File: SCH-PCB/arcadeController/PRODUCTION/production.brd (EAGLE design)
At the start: 120.9 x 92.9 mm, 52 parts, among them J1 1759046, J2 1759046, J3 1759046, J4 1759046, J5 1759046, J6 1759046, J7 1759046, J8 1759046, U1 RASPBERRY_PICOSMD-TH, U2 RASPBERRY_PICOSMD-TH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

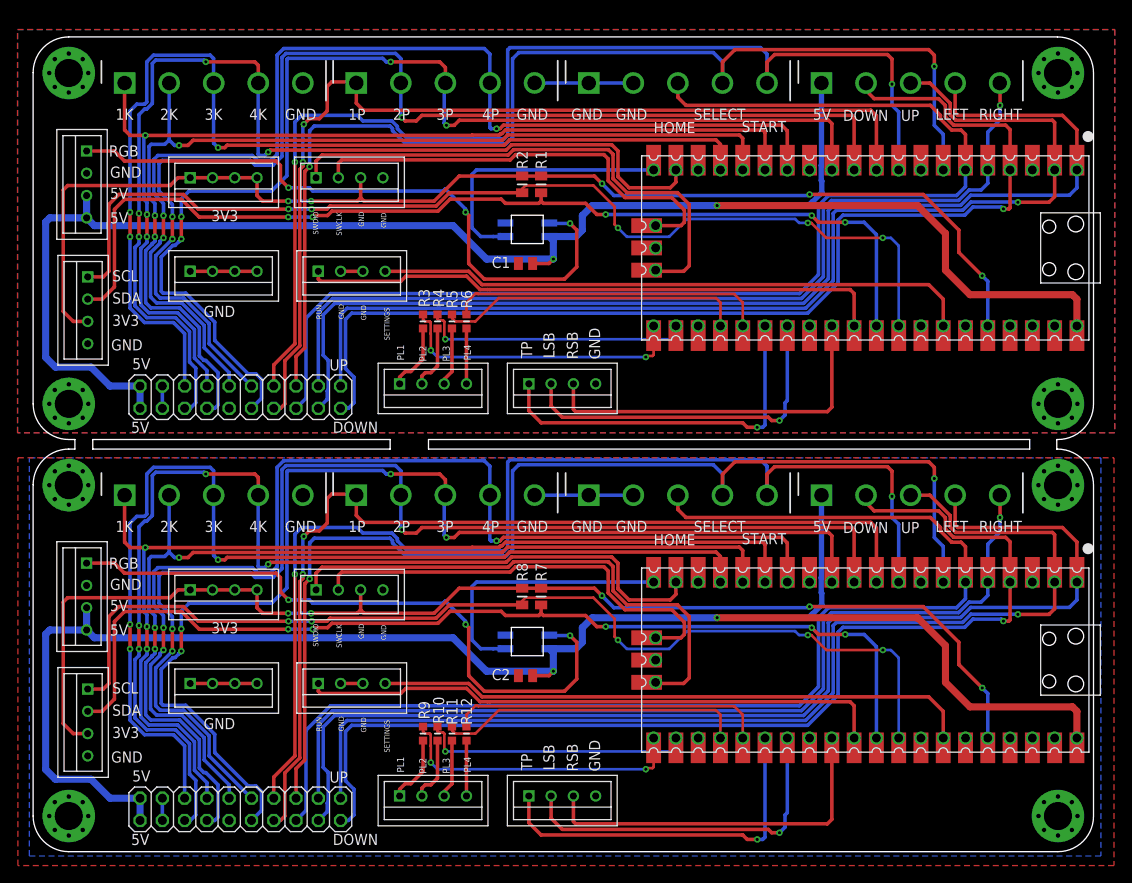
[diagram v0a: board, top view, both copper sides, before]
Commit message: FIX: PCB design there are line with <0.1mm
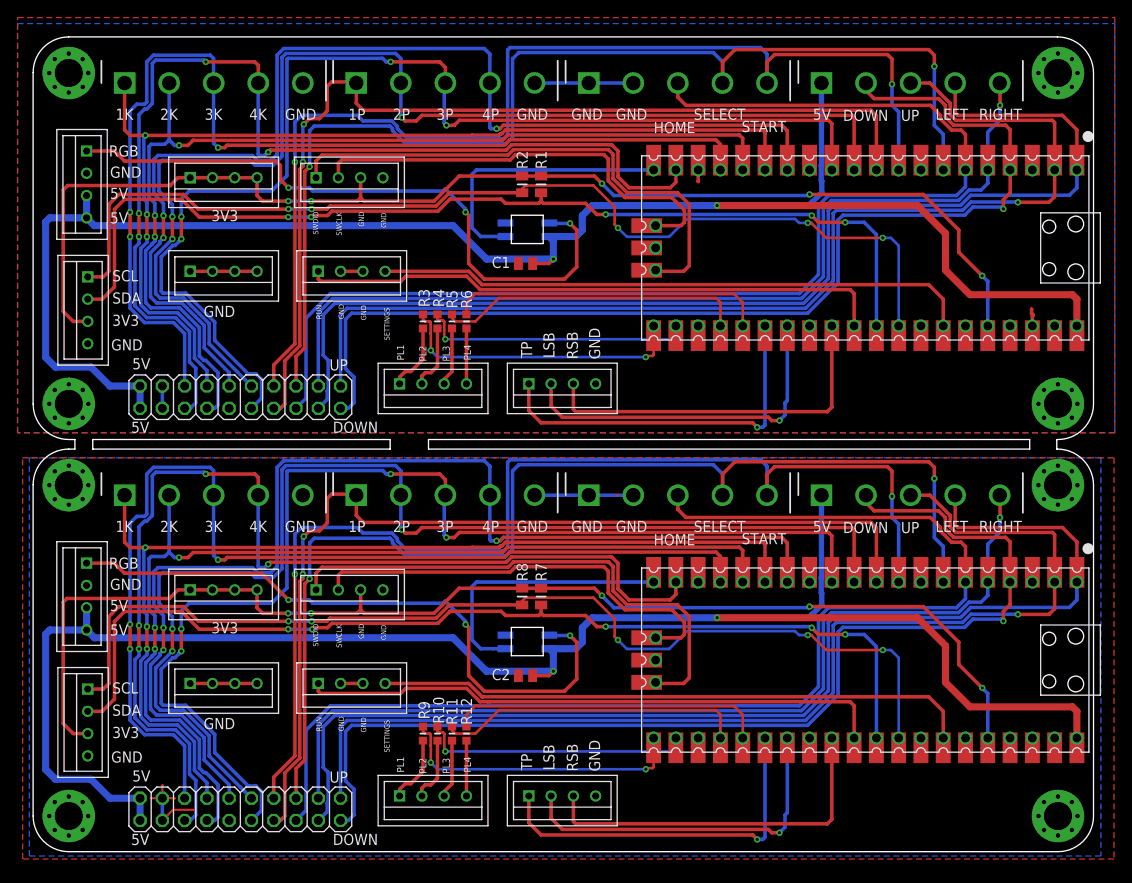
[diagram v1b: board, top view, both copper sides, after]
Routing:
- net GND1: track 24.0 -> 32.4 mm
- net GND: track 24.0 -> 31.8 mm
- net START: track 130.3 -> 131.4 mm
- net SELECT: track 131.4 -> 132.5 mm
- net VSYS: track 0.00 -> 1.11 mm
- net RIGHT: track 107.4 -> 108.5 mm
- net RGB: track 32.1 -> 33.2 mm
- net 3K: track 120.9 -> 122.0 mm
- net 2K: track 115.1 -> 116.2 mm
- net 1K: track 116.3 -> 117.4 mm
- net HOME: track 138.0 -> 139.1 mm
- net 1P: track 111.2 -> 112.3 mm
- net RGBOUT1: track 75.0 -> 74.1 mm
